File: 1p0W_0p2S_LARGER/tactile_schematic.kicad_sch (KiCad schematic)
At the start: 55 parts, among them IC1 CY8C4145PVI-PS431, J1 Conn_01x03, J2 Conn_01x04, J3 Conn_01x04, J4 Conn_01x03, J5 Conn_ARM_SWD_TagConnect_TC203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

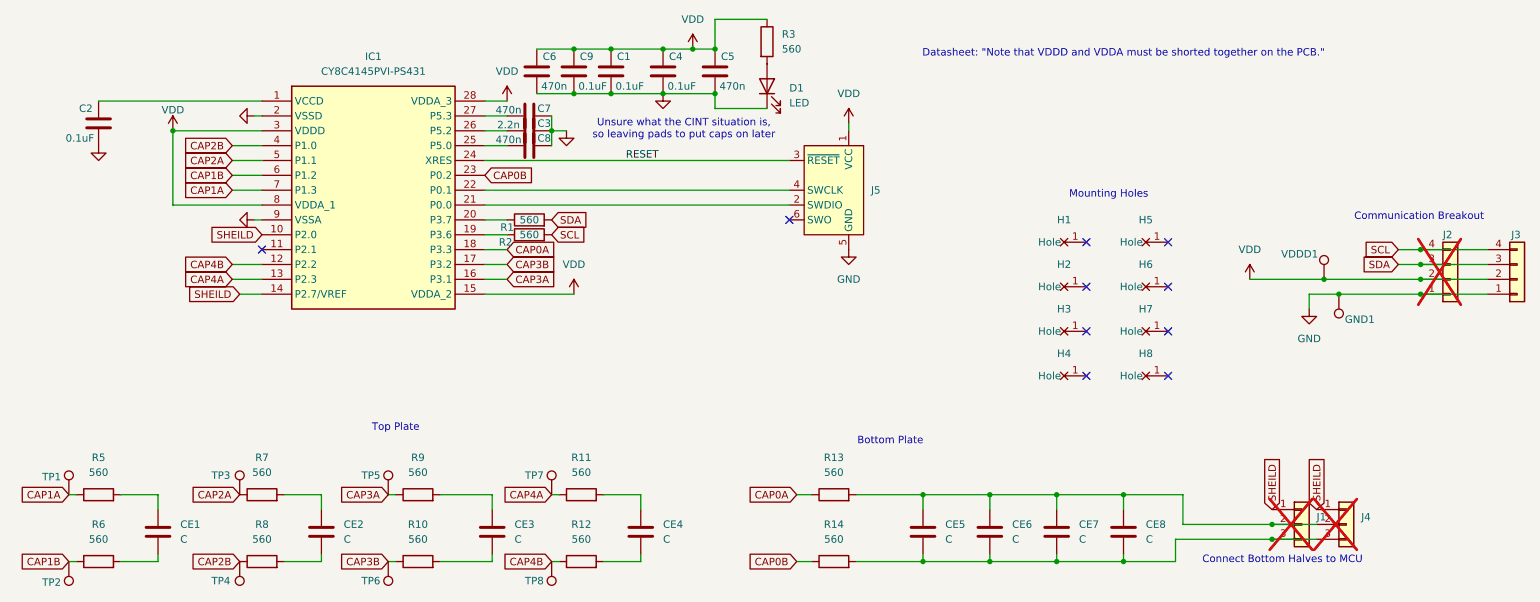
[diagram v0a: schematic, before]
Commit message: fixed silkscreen
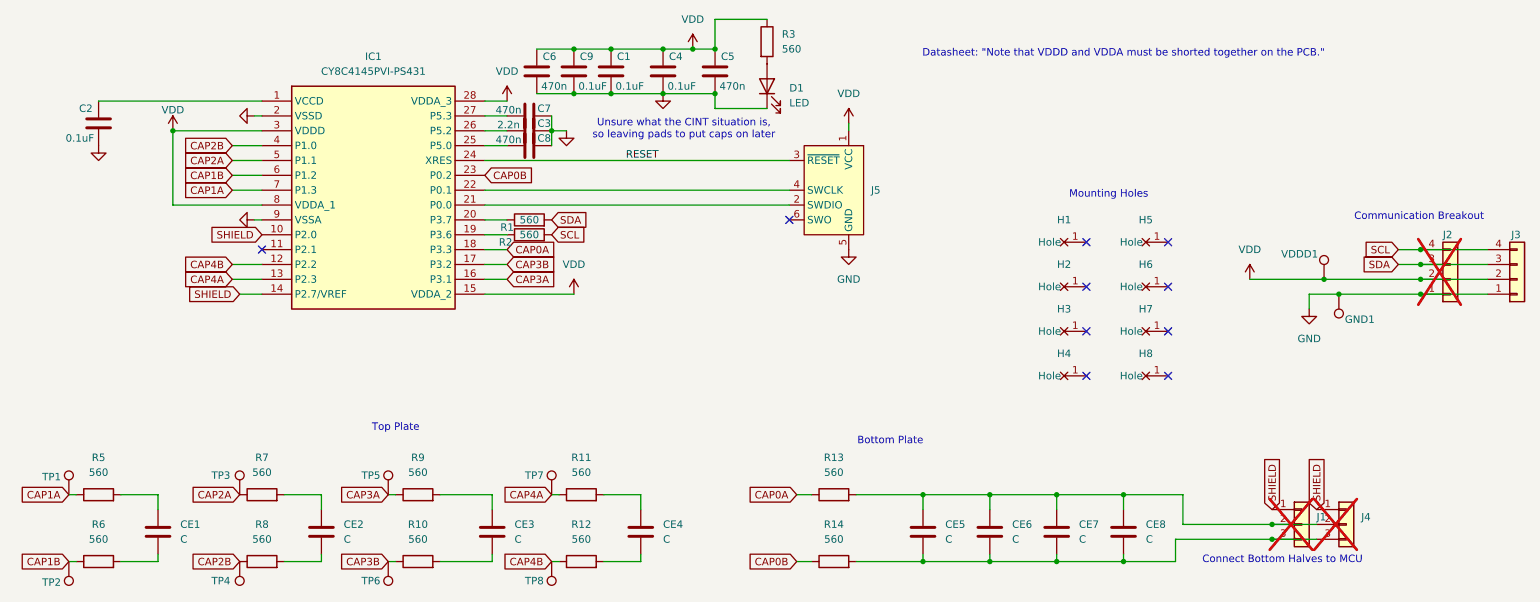
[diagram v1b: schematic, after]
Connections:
- net SHEILD renamed SHIELD
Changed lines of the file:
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@@
 		)
 	)
-	(global_label "SHEILD"
+	(global_label "SHIELD"
 		(shape input)
 		(at 228.6 99.06 90)
@@
 		)
 	)
-	(global_label "SHEILD"
+	(global_label "SHIELD"
 		(shape input)
 		(at 55.88 52.07 180)
@@
 		)
 	)
-	(global_label "SHEILD"
+	(global_label "SHIELD"
 		(shape input)
 		(at 52.07 62.23 180)
@@
 		)
 	)
-	(global_label "SHEILD"
+	(global_label "SHIELD"
 		(shape input)
 		(at 236.22 99.06 90)

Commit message: more spacing fixes
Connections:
- net SHIELD: no longer IC1.14 (P2.7/VREF)
- no-connect marks 10 -> 11
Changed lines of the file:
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@@
+	)
+	(no_connect
+		(at 55.88 62.23)
 	)
 	(no_connect
@@
 	(wire
 		(pts
-			(xy 52.07 62.23) (xy 55.88 62.23)
-		)
-		(stroke
-			(width 0)
-			(type default)
-		)
-	)
-	(wire
-		(pts
 			(xy 93.98 52.07) (xy 97.79 52.07)
 		)
@@
 			(effects
 				(font
-					(size 1.27 1.27)
-				)
-				(justify right)
-				(hide yes)
-			)
-		)
-	)
-	(global_label "SHIELD"
-		(shape input)
-		(at 52.07 62.23 180)
-		(fields_autoplaced yes)
-		(effects
-			(font
-				(size 1.27 1.27)
-			)
-			(justify right)
-		)
-		(property "Intersheetrefs" "${INTERSHEET_REFS}"
-			(at 42.4929 62.23 0)
-			(effects
-				(font
